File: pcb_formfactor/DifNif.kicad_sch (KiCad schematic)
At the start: 26 parts, among them J2 PROG, J4 HPLA_PORT, U1 ICE40HX4K-TQ144, U13 Teensy4_1, U2 SST26VF080A-104I/SN, X1 ASE-xxxMHz

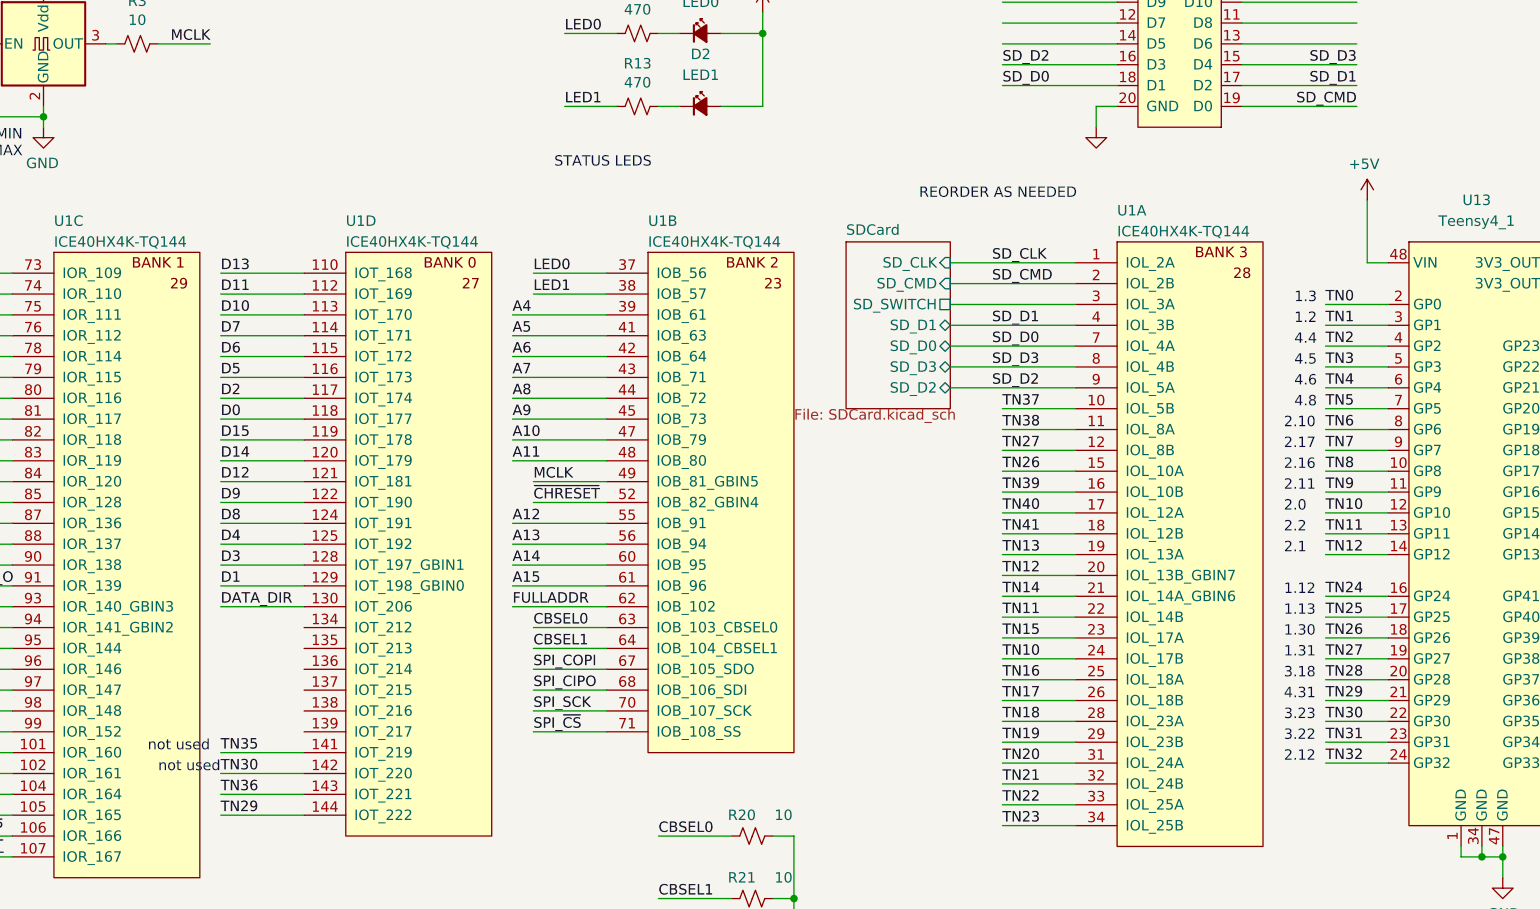
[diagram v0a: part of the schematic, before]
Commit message: Add diode OR, add clock series R
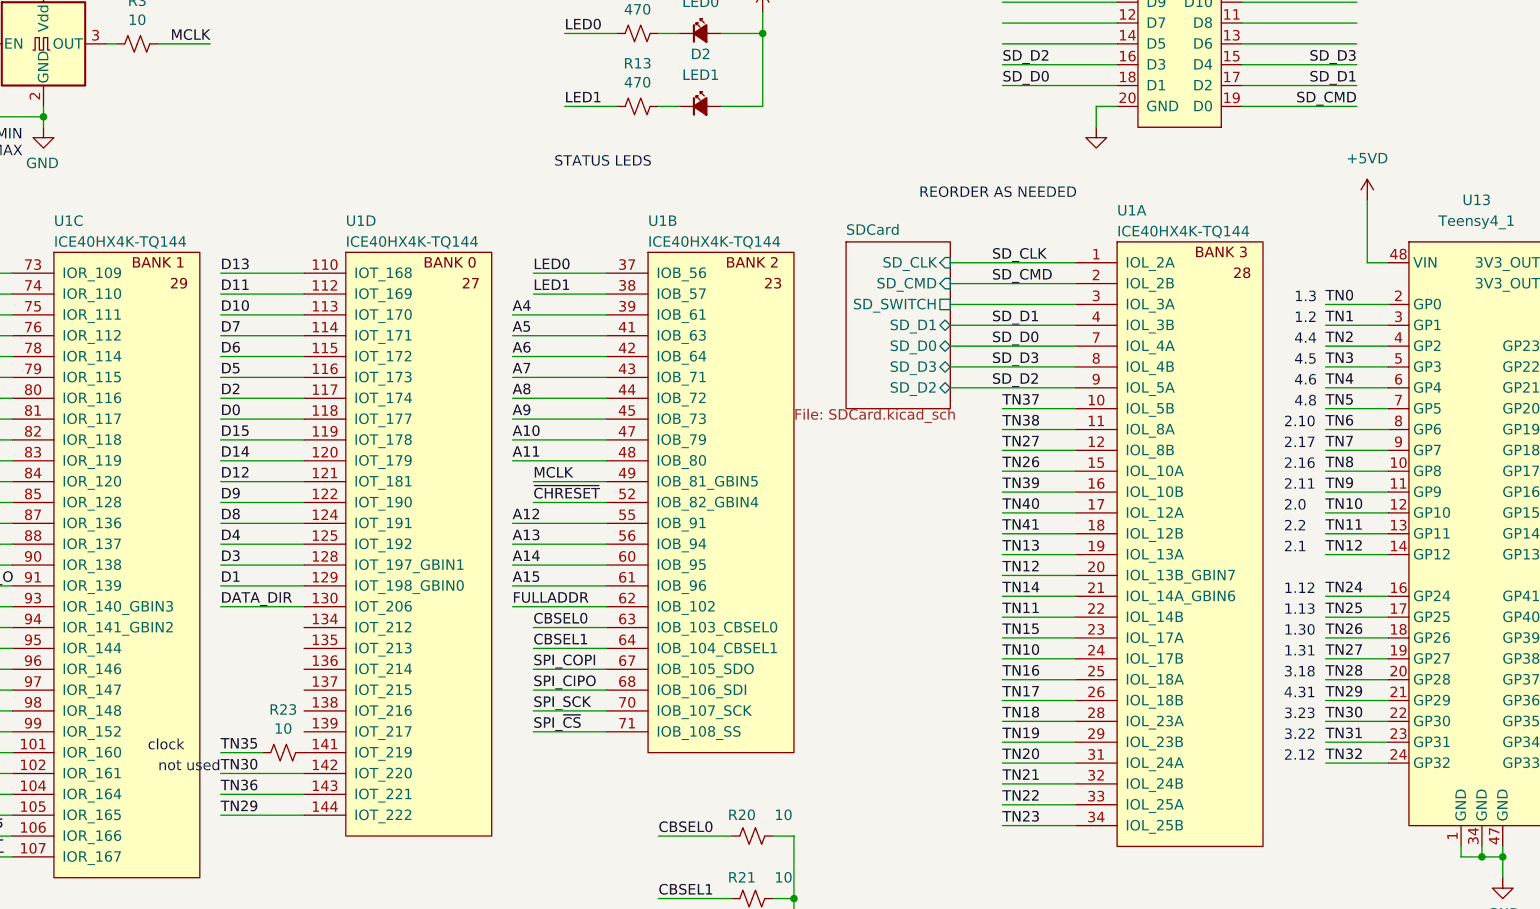
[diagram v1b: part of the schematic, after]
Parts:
- added R23: 10, Passive:RESC1608X55, symbol Device:R_Small_US
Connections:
- net TN35: now also R23.2; no longer U1.141 (IOT_219)
- net +5V renamed +5VD
- new net: R23.1, U1.141 (IOT_219)
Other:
- note added: "clock"
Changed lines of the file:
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@@
     (stroke (width 0) (type default) (color 0 0 0 0))
   )
-  (wire (pts (xy 106.68 121.92) (xy 116.84 121.92))
+  (wire (pts (xy 106.68 121.92) (xy 111.76 121.92))
     (stroke (width 0) (type default) (color 0 0 0 0))
   )
@@
     (effects (font (size 1.27 1.27)) (justify left bottom))
   )
-  (text "not used" (at 97.79 121.92 0)
+  (text "clock" (at 97.79 121.92 0)
     (effects (font (size 1.27 1.27)) (justify left bottom))
   )
@@
     (pin "2")
   )
+  (symbol (lib_id "Device:R_Small_US") (at 114.3 121.92 270) (unit 1)
+    (in_bom yes) (on_board yes)
+    (property "Reference" "R23" (id 0) (at 114.3 116.713 90))
+    (property "Value" "10" (id 1) (at 114.3 119.0244 90))
+    (property "Footprint" "Passive:RESC1608X55" (id 2) (at 114.3 121.92 0)
+      (effects (font (size 1.27 1.27)) hide)
+    )
+    (property "Datasheet" "~" (id 3) (at 114.3 121.92 0)
+      (effects (font (size 1.27 1.27)) hide)
+    )
+    (property "Mouser" "603-RC0603FR-0710RL" (id 4) (at 62.23 -6.35 0)
+      (effects (font (size 1.27 1.27)) hide)
+    )
+    (pin "1")
+    (pin "2")
+  )
   (symbol (lib_id "logic:ICE40HX4K-TQ144") (at 215.9 59.69 0) (unit 1)
     (in_bom yes) (on_board yes)
@@
     (pin "8")
   )
+  (symbol (lib_id "power:+5VD") (at 246.38 54.61 0) (unit 1)
+    (in_bom yes) (on_board yes) (fields_autoplaced)
+    (property "Reference" "#PWR011" (id 0) (at 246.38 58.42 0)
+      (effects (font (size 1.27 1.27)) hide)
+    )
+    (property "Value" "+5VD" (id 1) (at 246.38 49.53 0))
+    (property "Footprint" "" (id 2) (at 246.38 54.61 0)
+      (effects (font (size 1.27 1.27)) hide)
+    )
+    (property "Datasheet" "" (id 3) (at 246.38 54.61 0)
+      (effects (font (size 1.27 1.27)) hide)
+    )
+    (pin "1")
+  )
   (symbol (lib_id "Mechanical:MountingHole_Pad") (at 78.74 182.88 0) (unit 1)
     (in_bom yes) (on_board yes) (fields_autoplaced)
@@
     )
     (property "Datasheet" "" (id 3) (at 172.72 31.75 0)
-      (effects (font (size 1.27 1.27)) hide)
-    )
-    (pin "1")
-  )
-  (symbol (lib_id "power:+5V") (at 246.38 54.61 0) (mirror y) (unit 1)
-    (in_bom yes) (on_board yes)
-    (property "Reference" "#PWR011" (id 0) (at 246.38 58.42 0)
-      (effects (font (size 1.27 1.27)) hide)
-    )
-    (property "Value" "+5V" (id 1) (at 245.999 50.2158 0))
-    (property "Footprint" "" (id 2) (at 246.38 54.61 0)
-      (effects (font (size 1.27 1.27)) hide)
-    )
-    (property "Datasheet" "" (id 3) (at 246.38 54.61 0)
       (effects (font (size 1.27 1.27)) hide)
     )
@@
       (reference "#PWR010") (unit 1) (value "+3V3") (footprint "")
     )
-    (path "/f9b1fd47-53a9-4b8e-93ad-29781e05e37e"
-      (reference "#PWR011") (unit 1) (value "+5V") (footprint "")
+    (path "/d671ea80-46b4-4c76-8fdb-ef626bece258"
+      (reference "#PWR011") (unit 1) (value "+5VD") (footprint "")
     )
     (path "/894e4742-c535-4b25-876b-aca8c621e9fb"
@@
       (reference "#PWR016") (unit 1) (value "GND") (footprint "")
     )
+    (path "/f4193393-2cc9-4286-85ab-d00d3620a7d2/f71cdeb2-e88c-46fd-9bca-790eca942cd5"
+      (reference "#PWR017") (unit 1) (value "+5V") (footprint "")
+    )
+    (path "/f4193393-2cc9-4286-85ab-d00d3620a7d2/82d6cc08-4f1f-47c2-8f65-ccda8c835038"
+      (reference "#PWR018") (unit 1) (value "+5VD") (footprint "")
+    )
+    (path "/f4193393-2cc9-4286-85ab-d00d3620a7d2/5c2054fb-8f82-4af4-88a9-ea1b20540e16"
+      (reference "#PWR019") (unit 1) (value "+5VD") (footprint "")
+    )
+    (path "/f4193393-2cc9-4286-85ab-d00d3620a7d2/9a68a24b-bdf8-49fc-8e7c-909dd654cb30"
+      (reference "#PWR020") (unit 1) (value "+5VD") (footprint "")
+    )
     (path "/19b8b40d-8ec2-4dbf-9b1c-df901e2aebee"
       (reference "#PWR0101") (unit 1) (value "GND") (footprint "")
@@
       (reference "#PWR0115") (unit 1) (value "GND") (footprint "")
     )
-    (path "/f4193393-2cc9-4286-85ab-d00d3620a7d2/0a43c551-dbfe-43ff-a241-076a8ca91cef"
-      (reference "#PWR0116") (unit 1) (value "+5V") (footprint "")
-    )
     (path "/f4193393-2cc9-4286-85ab-d00d3620a7d2/a828edb3-dd7a-4b2d-a55e-eccfddbf1beb"
       (reference "#PWR0117") (unit 1) (value "GND") (footprint "")
@@
       (reference "#PWR0118") (unit 1) (value "GND") (footprint "")
     )
-    (path "/f4193393-2cc9-4286-85ab-d00d3620a7d2/116367b2-3e55-4ca0-83b2-aa471262d58c"
-      (reference "#PWR0119") (unit 1) (value "+5V") (footprint "")
-    )
     (path "/f4193393-2cc9-4286-85ab-d00d3620a7d2/cbedcb1f-f6fd-4ef5-b1b7-a22936804498"
       (reference "#PWR0120") (unit 1) (value "+3V3") (footprint "")
@@
       (reference "D2") (unit 1) (value "LED1") (footprint "Active:LEDM1608X50")
     )
+    (path "/f4193393-2cc9-4286-85ab-d00d3620a7d2/87f2dc0e-0fb0-4ff1-8581-5f9863f598c2"
+      (reference "D3") (unit 1) (value "PMEG10010ELR") (footprint "Active:SOD3716X117")
+    )
     (path "/55336152-d16d-4e15-8a84-c366eb347710"
       (reference "H1") (unit 1) (value "MountingHole_Pad") (footprint "MountingHole:MountingHole_2.7mm_Pad")
@@
       (reference "R22") (unit 1) (value "10") (footprint "Passive:RESC1608X55")
     )
+    (path "/afb97014-e551-4ba6-b5c5-3015815c1e36"
+      (reference "R23") (unit 1) (value "10") (footprint "Passive:RESC1608X55")
+    )
     (path "/b7cdbf56-648f-4b61-a929-f6df4844931e"

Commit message: fabout form factor pcb
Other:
- moved on the sheet: R23
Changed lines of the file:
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@@
+    (stroke (width 0) (type default) (color 0 0 0 0))
+  )
+  (wire (pts (xy 115.57 121.92) (xy 116.84 121.92))
     (stroke (width 0) (type default) (color 0 0 0 0))
   )
@@
     (stroke (width 0) (type default) (color 0 0 0 0))
   )
-  (wire (pts (xy 106.68 121.92) (xy 111.76 121.92))
+  (wire (pts (xy 105.41 121.92) (xy 110.49 121.92))
     (stroke (width 0) (type default) (color 0 0 0 0))
   )
@@
     (effects (font (size 1.27 1.27)) (justify right bottom))
   )
-  (label "TN35" (at 106.68 121.92 0)
+  (label "TN35" (at 105.41 121.92 0)
     (effects (font (size 1.27 1.27)) (justify left bottom))
   )
@@
     (pin "2")
   )
-  (symbol (lib_id "Device:R_Small_US") (at 114.3 121.92 270) (unit 1)
-    (in_bom yes) (on_board yes)
-    (property "Reference" "R23" (id 0) (at 114.3 116.713 90))
-    (property "Value" "10" (id 1) (at 114.3 119.0244 90))
-    (property "Footprint" "Passive:RESC1608X55" (id 2) (at 114.3 121.92 0)
-      (effects (font (size 1.27 1.27)) hide)
-    )
-    (property "Datasheet" "~" (id 3) (at 114.3 121.92 0)
-      (effects (font (size 1.27 1.27)) hide)
-    )
-    (property "Mouser" "603-RC0603FR-0710RL" (id 4) (at 62.23 -6.35 0)
-      (effects (font (size 1.27 1.27)) hide)
-    )
+  (symbol (lib_id "Device:R_Small_US") (at 113.03 121.92 270) (unit 1)
+    (in_bom yes) (on_board yes)
+    (property "Reference" "R23" (id 0) (at 113.03 116.713 90))
+    (property "Value" "10" (id 1) (at 113.03 119.0244 90))
+    (property "Footprint" "Passive:RESC1608X55" (id 2) (at 113.03 121.92 0)
+      (effects (font (size 1.27 1.27)) hide)
+    )
+    (property "Datasheet" "~" (id 3) (at 113.03 121.92 0)
+      (effects (font (size 1.27 1.27)) hide)
+    )
+    (property "Mouser" "603-RC0603FR-0710RL" (id 4) (at 60.96 -6.35 0)
+      (effects (font (size 1.27 1.27)) hide)
+    )
